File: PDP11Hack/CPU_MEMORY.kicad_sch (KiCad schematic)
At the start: 19 parts, among them SW1 SW_Push, SW2 SW_Push, U10 628128_DIP32_SSOP32, U11 628128_DIP32_SSOP32, U12 74LS00, U2 74LS273, U3 74LS273, U4 74LS04, U9 74LS139, Y1 Crystal

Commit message: Finished schematic
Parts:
- added U4: 74LS04, symbol 74xx:74LS04

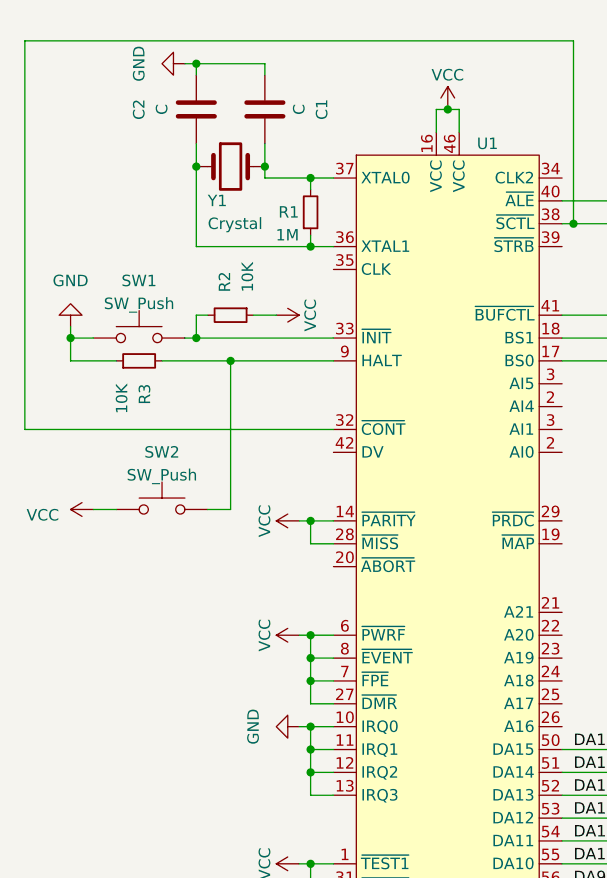
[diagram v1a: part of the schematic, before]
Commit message: Assigned footprints.
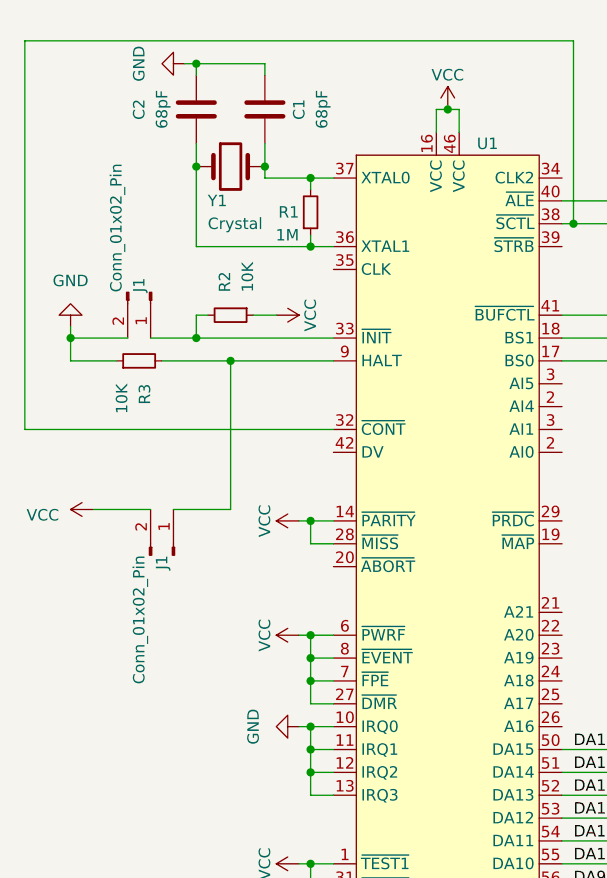
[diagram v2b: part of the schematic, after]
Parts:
- removed SW1, SW2: SW_Push, symbol Switch:SW_Push
- added J1 (x2): Conn_01x02_Pin, Connector_PinHeader_1.27mm:PinHeader_1x02_P1.27mm_Vertical, symbol Connector:Conn_01x02_Pin
- C1, C2: value C -> 68pF; footprint (none) -> Capacitor_THT:C_Disc_D3.0mm_W2.0mm_P2.50mm
- R1, R2, R3: footprint (none) -> Resistor_THT:R_Axial_DIN0207_L6.3mm_D2.5mm_P7.62mm_Horizontal
- U1: footprint (none) -> DCJ11:DCJ11-AE
- U10, U11: footprint (none) -> Package_DIP:DIP-32_W15.24mm
- U12, U4: footprint (none) -> Package_DIP:DIP-14_W7.62mm
- U2, U3: footprint (none) -> Package_DIP:DIP-20_W7.62mm
- U9: footprint (none) -> Package_DIP:DIP-16_W7.62mm
- Y1: footprint (none) -> Crystal:Crystal_HC49-4H_Vertical
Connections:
- net GND: now also J1.2 (Pin_2)
- net VCC: now also J1.2 (Pin_2)
- net at R3.2, U1.9 (HALT): now also J1.1 (Pin_1)
- net at R2.2, U1.33 (~{INIT}): now also J1.1 (Pin_1)
